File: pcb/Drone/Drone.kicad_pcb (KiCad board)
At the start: 2 copper layers, 72 x 72 mm, 52 parts, among them J1 USB_C_Receptacle_USB2.0_16P, J10 JST1.25, J2 JST1.25, J3 JST1.25, J4 JST1.25, J5 JST1.25, J6 JST1.25, J7 JST1.25, J8 JST1.25, J9 JST1.25, Q1 SS8050, Q2 SS8050, Q3 Si2301, SW1 RST, SW2 BOOT, U1 esp32s3_wroom1, U2 DW01A, U4 USBLC6-2SC6, U5 8205, U6 CP2102, U8 ME6211C33M5

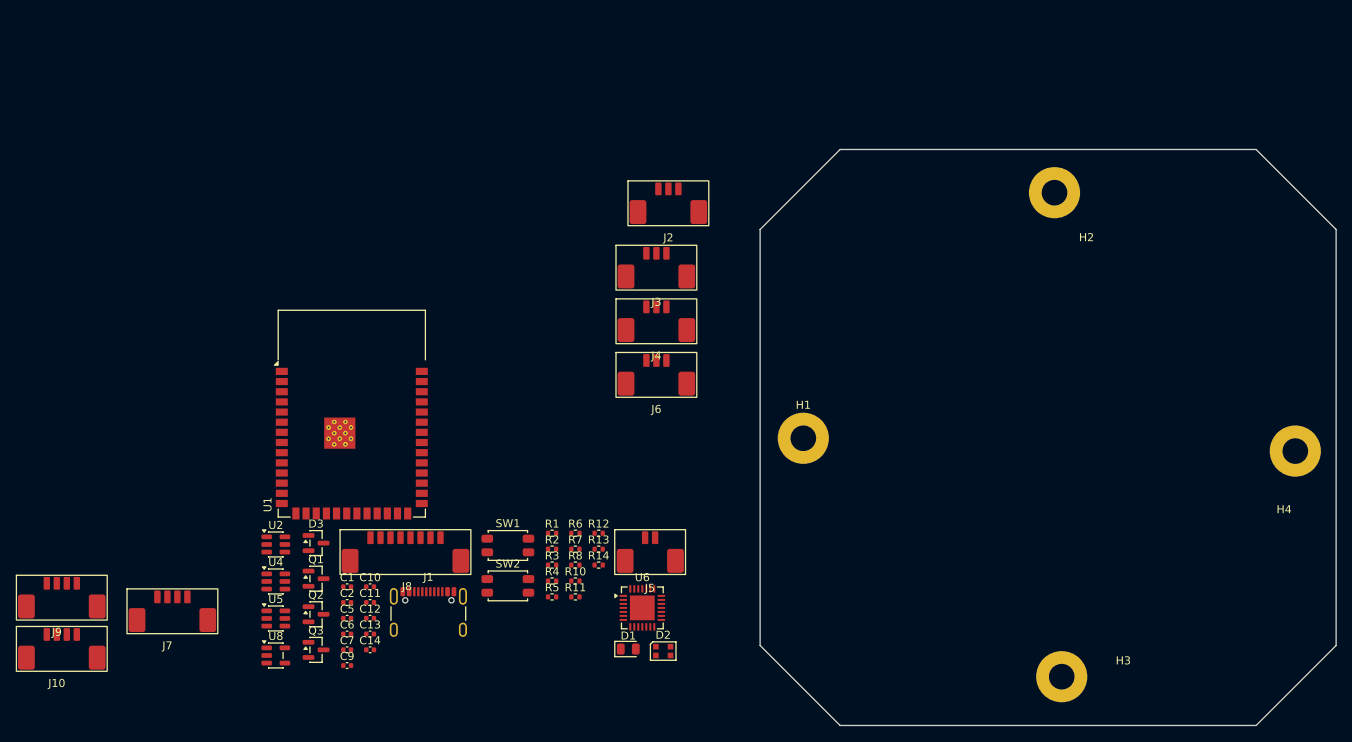
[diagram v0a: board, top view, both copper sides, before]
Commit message: power rail splitting
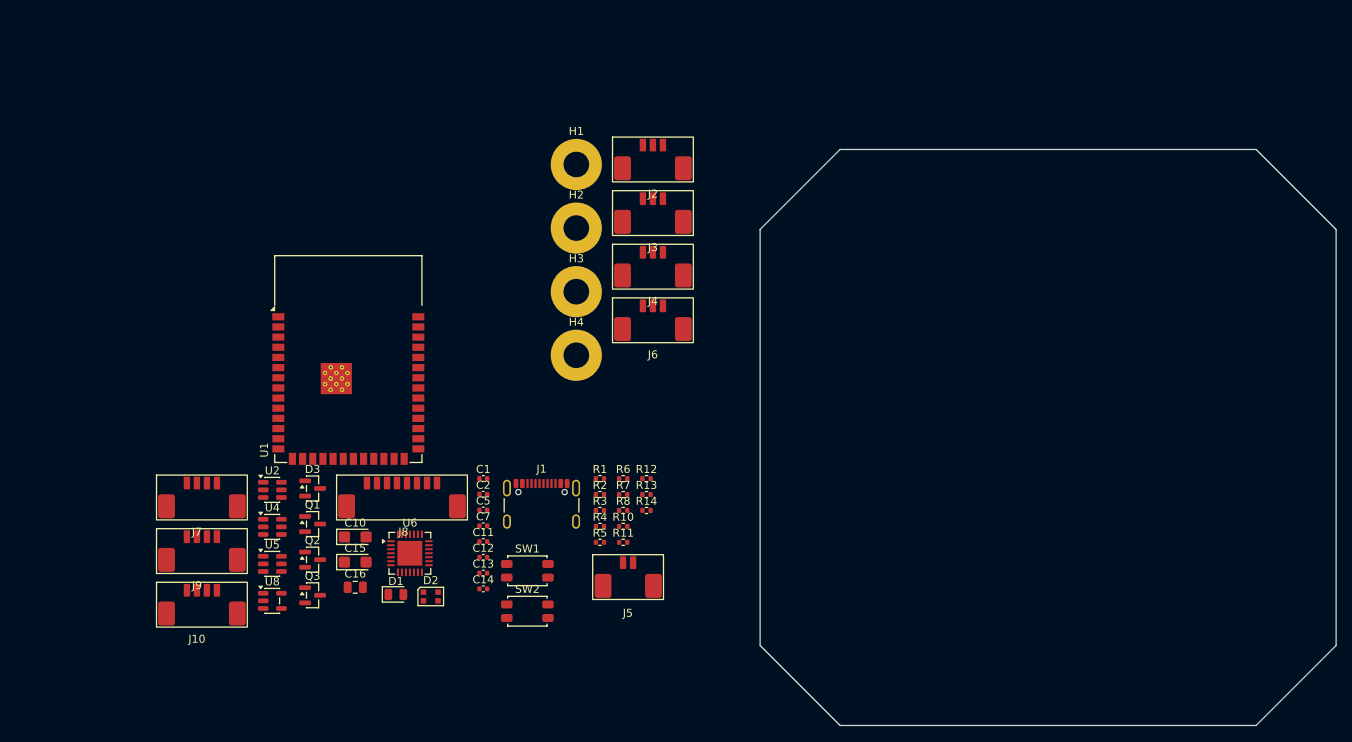
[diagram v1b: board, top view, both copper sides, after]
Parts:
- removed C6: 1u, Capacitor_SMD:C_0402_1005Metric
- removed C9: 22u, Capacitor_SMD:C_0402_1005Metric
- added C15: 100u, Capacitor_Tantalum_SMD:CP_EIA-3216-10_Kemet-I, F.Cu at (71.6, 110.1)
- added C16: 22u, Capacitor_SMD:C_0805_2012Metric, F.Cu at (71.6, 113.2)
- C10: footprint Capacitor_SMD:C_0402_1005Metric -> Capacitor_Tantalum_SMD:CP_EIA-3216-10_Kemet-I
- moved H4 90.7 mm to (99.2, 84.2)
- moved H3 77.4 mm to (99.2, 76.3)
- moved H2 59.9 mm to (99.2, 68.3)
- moved H1 44.5 mm to (99.2, 60.4)
- moved D1 29.8 mm to (76.7, 114.1)
- moved D2 29.8 mm to (81.0, 114.4)
- moved U6 29.8 mm to (78.4, 109.0)
- moved C7 23.0 mm to (87.6, 105.5)
- moved C1 21.7 mm to (87.6, 99.6)
- moved C2 21.7 mm to (87.6, 101.6)
- moved C5 21.7 mm to (87.6, 103.6)
- moved J1 19.6 mm to (94.9, 103.9)
- moved J9 18.5 mm to (50.5, 106.9)
- moved J10 18.4 mm to (50.5, 113.6)
- moved C14 16.1 mm to (87.6, 113.4)
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
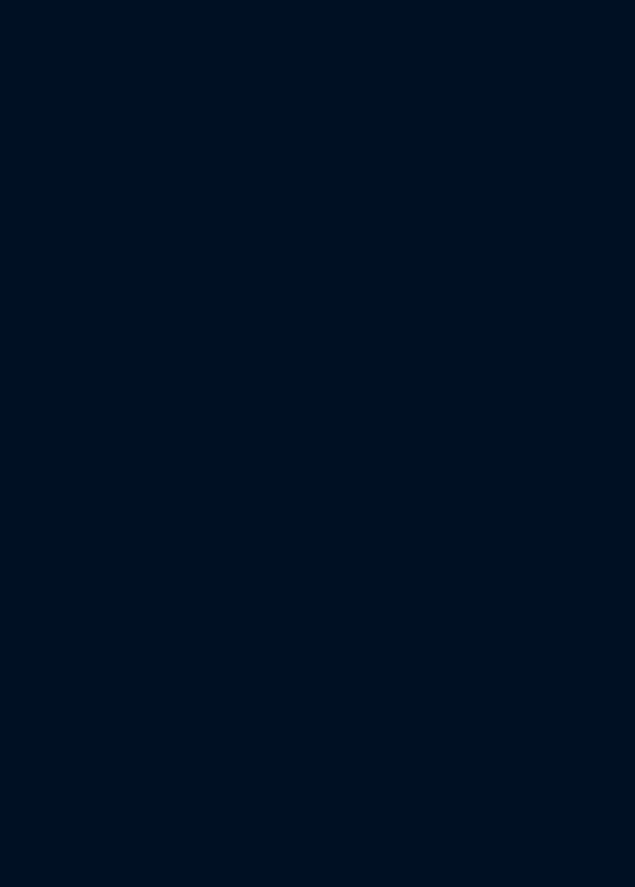
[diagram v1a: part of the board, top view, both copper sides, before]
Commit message: [analyze] finish mag with pin interrupt
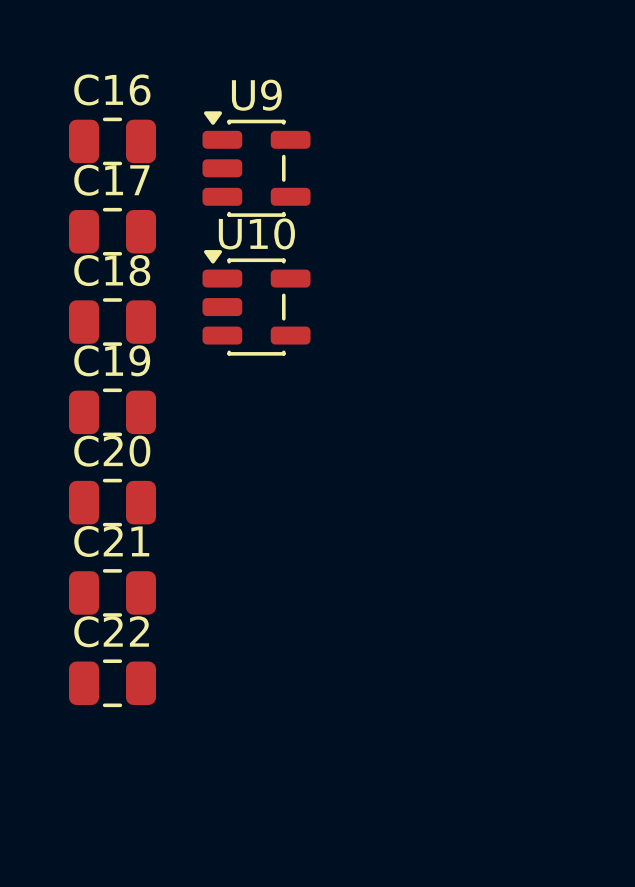
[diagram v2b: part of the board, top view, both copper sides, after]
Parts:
- added C16: 22u, Capacitor_SMD:C_0805_2012Metric, F.Cu at (41.1, 44.5)
- added C17: 10u, Capacitor_SMD:C_0805_2012Metric, F.Cu at (41.1, 47.5)
- added C18: 22u, Capacitor_SMD:C_0805_2012Metric, F.Cu at (41.1, 50.5)
- added C19: 10u, Capacitor_SMD:C_0805_2012Metric, F.Cu at (41.1, 53.6)
- added C20: 0.1u, Capacitor_SMD:C_0805_2012Metric, F.Cu at (41.1, 56.6)
- added C21: 0.1u, Capacitor_SMD:C_0805_2012Metric, F.Cu at (41.1, 59.6)
- added C22: 0.1u, Capacitor_SMD:C_0805_2012Metric, F.Cu at (41.1, 62.6)
- added U10: AP2112K-3.3, Package_TO_SOT_SMD:SOT-23-5, F.Cu at (45.9, 50.0)
- added U9: ME6211C33M5, Package_TO_SOT_SMD:SOT-23-5, F.Cu at (45.9, 45.4)
